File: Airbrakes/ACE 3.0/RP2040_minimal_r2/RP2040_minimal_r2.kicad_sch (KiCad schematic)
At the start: 45 parts, among them J1 USB_B_Micro, J2 Conn_01x02, J3 104031-0811, J4 Conn_02x18_Odd_Even, J5 104031-0811, U1 NCP1117-3.3_SOT223, U2 W25Q128JVS, U3 RP2040, U4 BMI088, U5 BMP581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

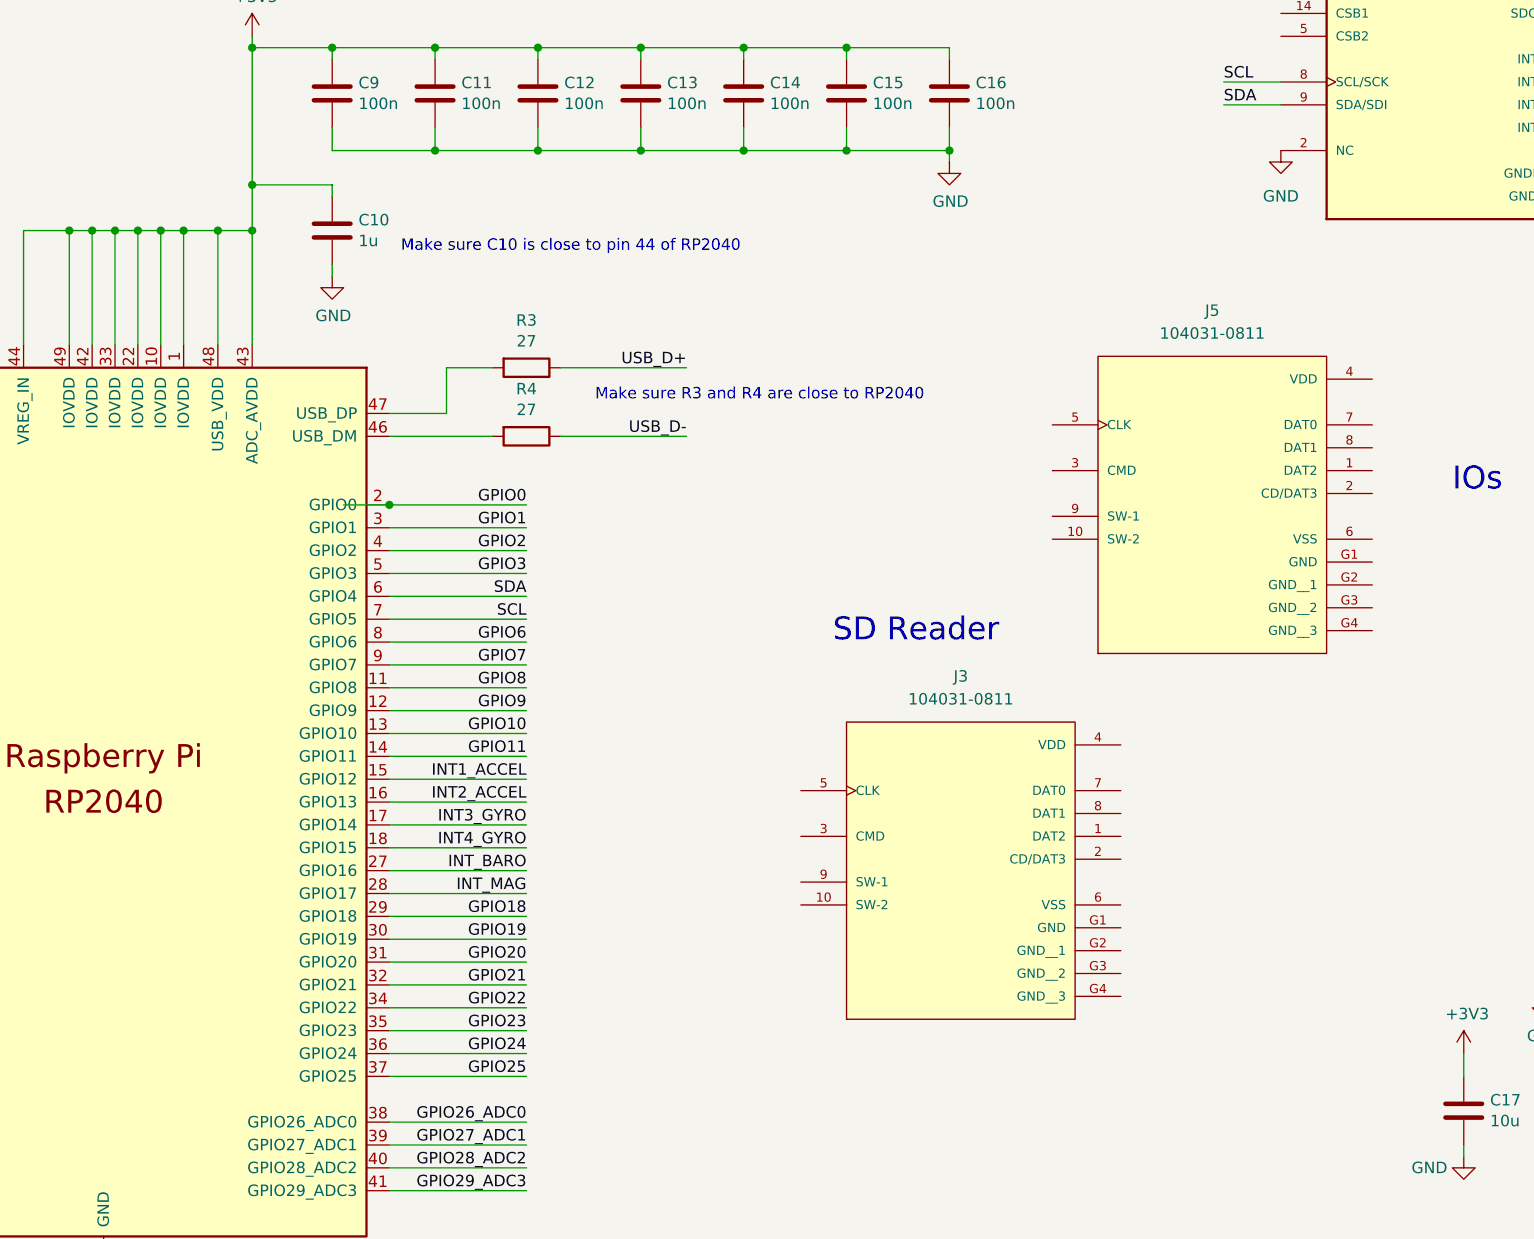
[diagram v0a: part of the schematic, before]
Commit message: sd card interfacing
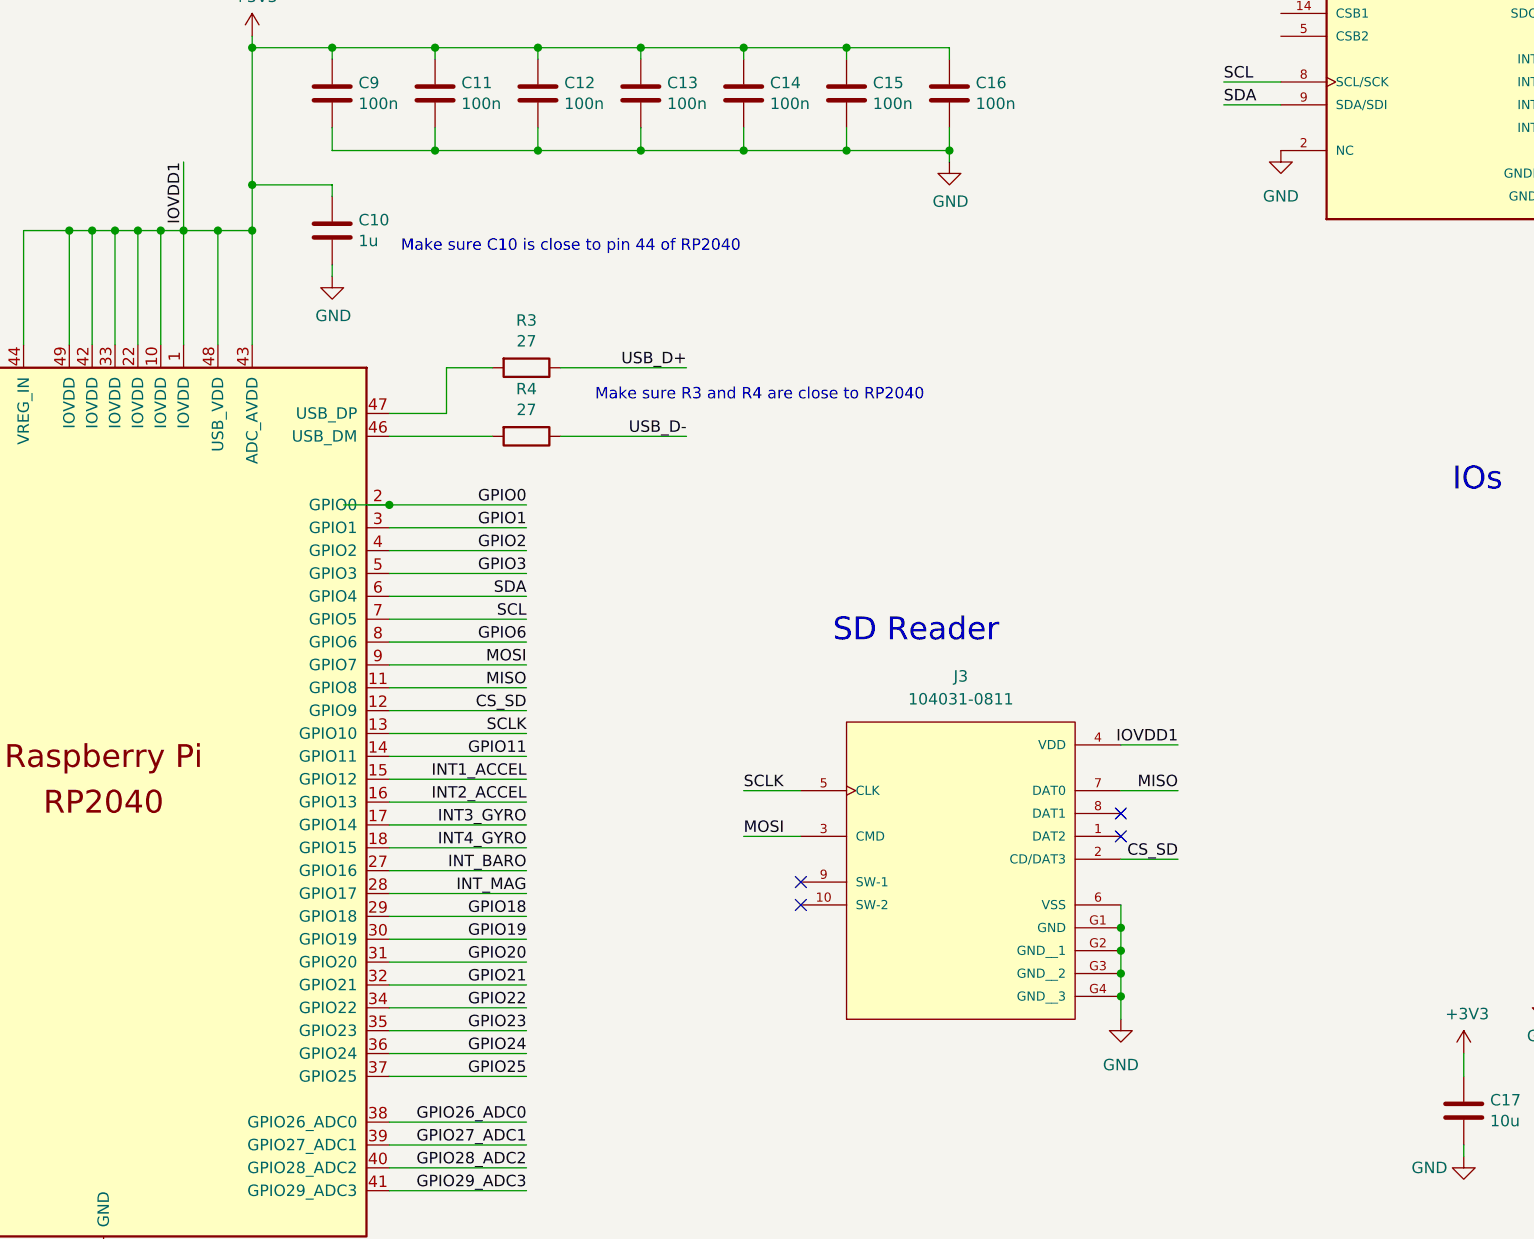
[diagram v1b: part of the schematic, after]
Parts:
- removed J5: 104031-0811, 1040310811-molex_usb:MOLEX_104031-0811, symbol 104031-0811:104031-0811
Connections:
- net GPIO10 is gone; now on net SCLK: U3.13 (GPIO10)
- net GPIO7 is gone; now on net MOSI: U3.9 (GPIO7)
- net GPIO8 is gone; now on net MISO: U3.11 (GPIO8)
- net GPIO9 is gone; now on net CS_SD: U3.12 (GPIO9)
- net +3V3: now also J3.4 (VDD)
- net GND: now also J3.6 (VSS), J3.G1 (GND), J3.G2 (GND__1), J3.G3 (GND__2), J3.G4 (GND__3)
- net CS_SD: now reaches J3.2 (CD/DAT3)
- net MOSI: now reaches J3.3 (CMD)
- net SCLK: now reaches J3.5 (CLK)
- net MISO: now reaches J3.7 (DAT0)
- no-connect marks 1 -> 5

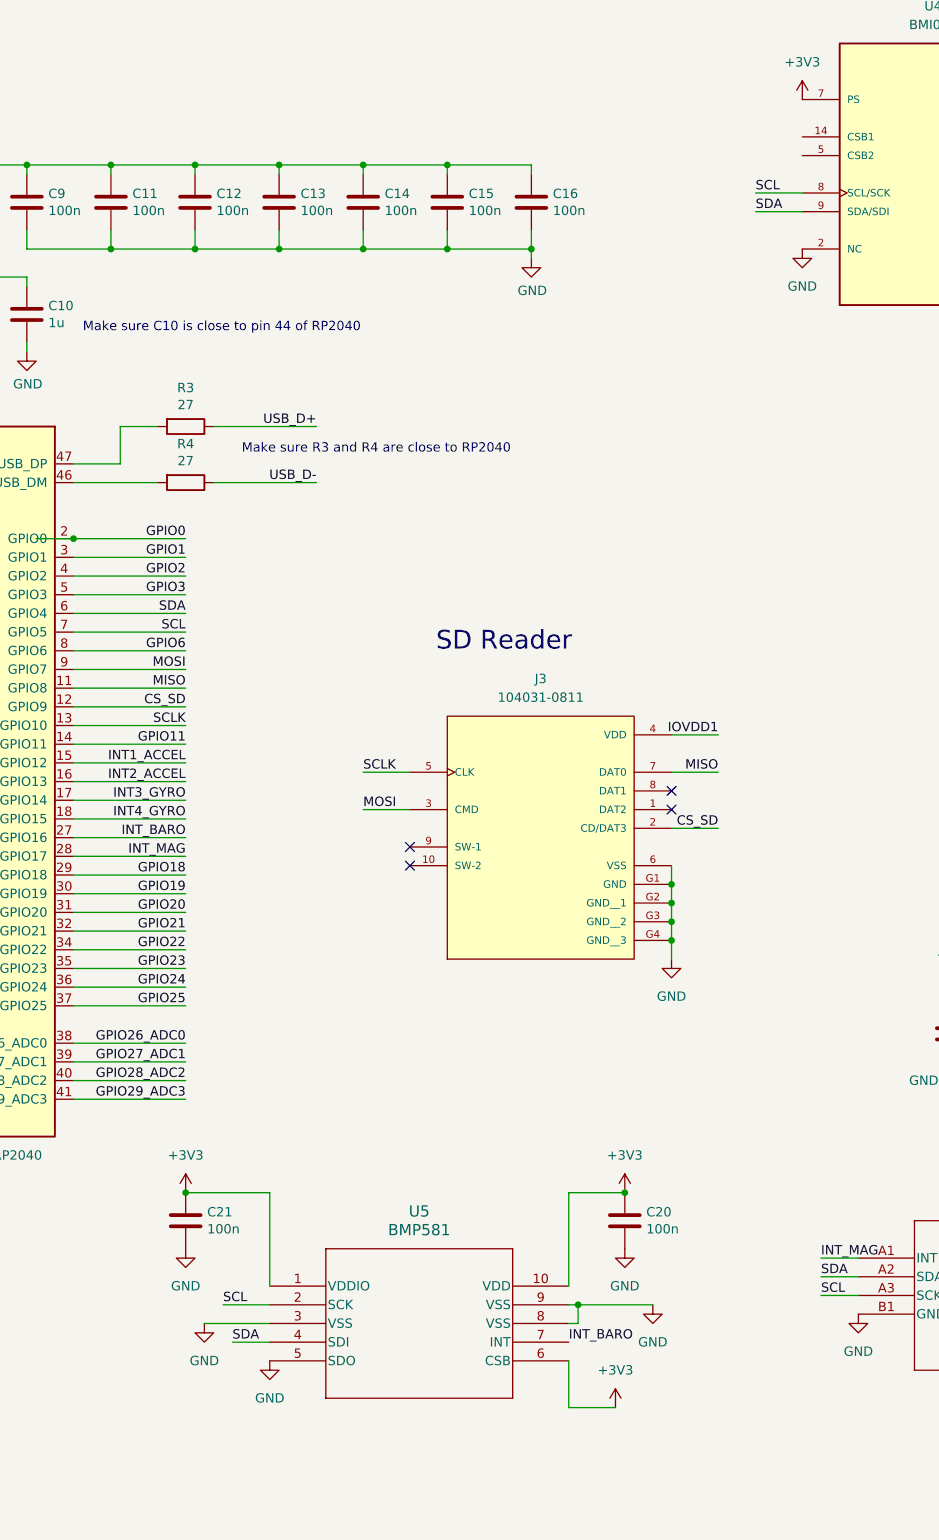
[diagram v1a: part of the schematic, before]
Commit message: changed cs_sd to pull-up and fixed csb
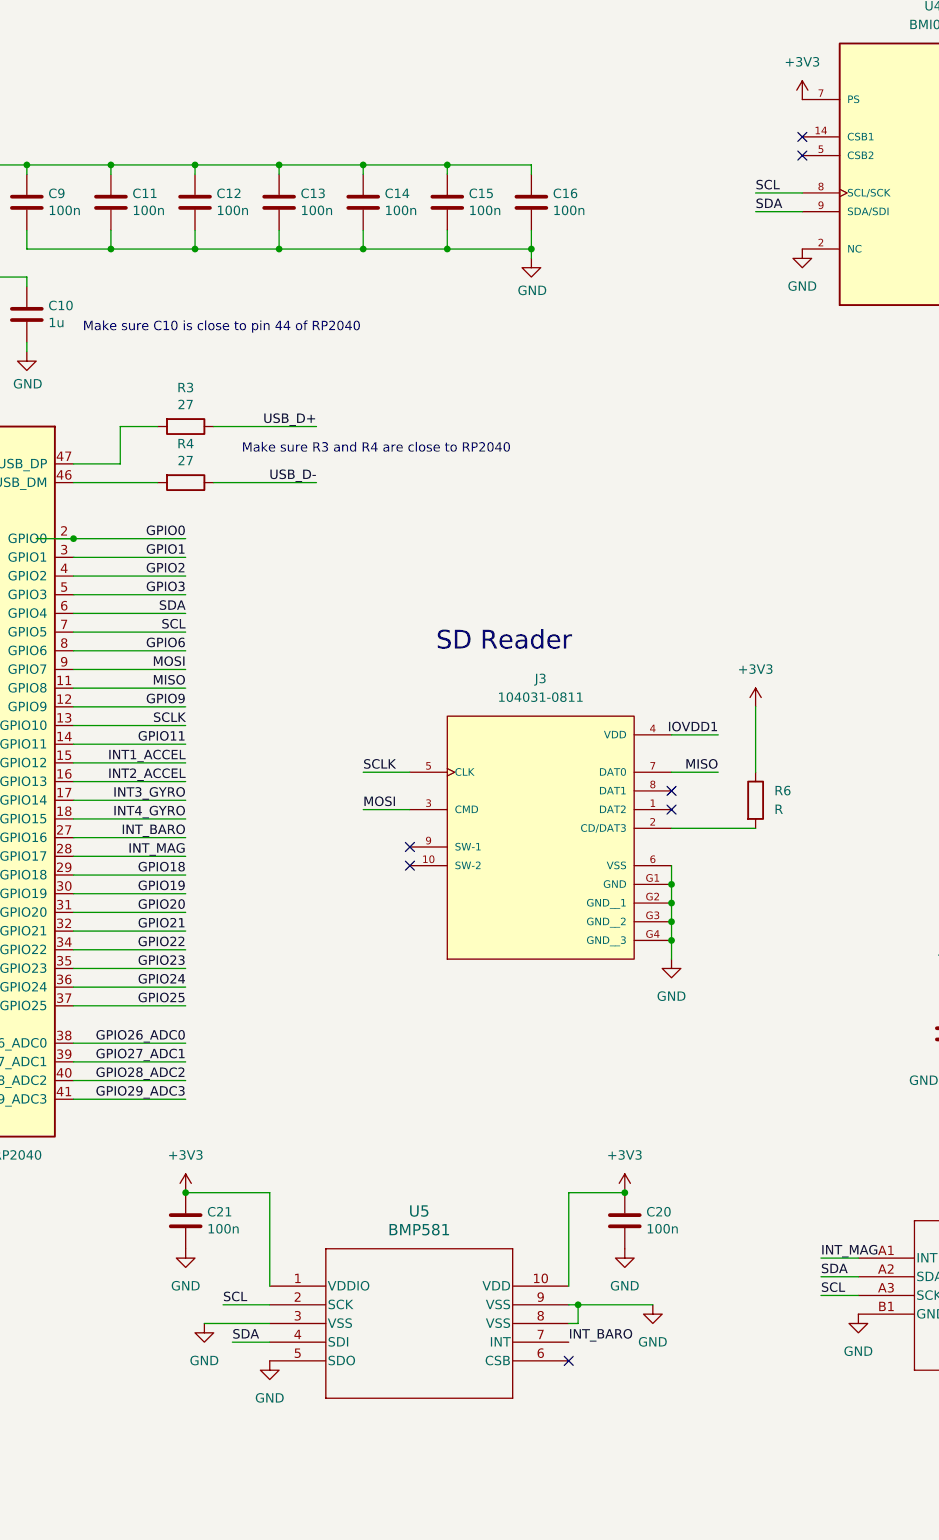
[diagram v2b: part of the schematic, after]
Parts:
- added R6: R, Resistor_SMD:R_0402_1005Metric, symbol Device:R
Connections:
- net +3V3: now also R6.1; no longer U5.6 (CSB)
- net CS_SD: no longer names the net of J3.2 (CD/DAT3)
- net CS_SD: now also R6.2; no longer U3.12 (GPIO9)
- new net GPIO9: U3.12 (GPIO9)
- no-connect marks 5 -> 8
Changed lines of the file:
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@@
 	)
 	(no_connect
+		(at 297.18 223.52)
+	)
+	(no_connect
 		(at 311.15 148.59)
 	)
@@
 	)
 	(no_connect
+		(at 328.93 57.15)
+	)
+	(no_connect
+		(at 328.93 59.69)
+	)
+	(no_connect
 		(at 311.15 146.05)
 	)
@@
 	(wire
 		(pts
-			(xy 297.18 223.52) (xy 297.18 229.87)
-		)
-		(stroke
-			(width 0)
-			(type default)
-		)
-	)
-	(wire
-		(pts
 			(xy 384.81 124.46) (xy 384.81 127)
 		)
@@
 	(wire
 		(pts
+			(xy 322.58 134.62) (xy 322.58 143.51)
+		)
+		(stroke
+			(width 0)
+			(type default)
+		)
+	)
+	(wire
+		(pts
 			(xy 297.18 215.9) (xy 298.45 215.9)
 		)
@@
 	(wire
 		(pts
-			(xy 297.18 229.87) (xy 303.53 229.87)
-		)
-		(stroke
-			(width 0)
-			(type default)
-		)
-	)
-	(wire
-		(pts
 			(xy 168.91 76.2) (xy 177.8 76.2)
 		)
@@
 	(wire
 		(pts
-			(xy 311.15 151.13) (xy 317.5 151.13)
+			(xy 311.15 151.13) (xy 322.58 151.13)
 		)
 		(stroke
@@
 		)
 	)
-	(label "CS_SD"
-		(at 317.5 151.13 180)
-		(fields_autoplaced yes)
-		(effects
-			(font
-				(size 1.27 1.27)
-			)
-			(justify right bottom)
-		)
-	)
 	(label "QSPI_SD2"
 		(at 152.4 121.92 0)
@@
 		)
 	)
-	(label "CS_SD"
+	(label "GPIO9"
 		(at 245.11 134.62 180)
 		(fields_autoplaced yes)
@@
 	)
 	(symbol
+		(lib_id "Device:R")
+		(at 322.58 147.32 0)
+		(unit 1)
+		(exclude_from_sim no)
+		(in_bom yes)
+		(on_board yes)
+		(dnp no)
+		(fields_autoplaced yes)
+		(property "Reference" "R6"
+			(at 325.12 146.0499 0)
+			(effects
+				(font
+					(size 1.27 1.27)
+				)
+				(justify left)
+			)
+		)
+		(property "Value" "R"
+			(at 325.12 148.5899 0)
+			(effects
+				(font
+					(size 1.27 1.27)
+				)
+				(justify left)
+			)
+		)
+		(property "Footprint" "Resistor_SMD:R_0402_1005Metric"
+			(at 320.802 147.32 90)
+			(effects
+				(font
+					(size 1.27 1.27)
+				)
+				(hide yes)
+			)
+		)
+		(property "Datasheet" "~"
+			(at 322.58 147.32 0)
+			(effects
+				(font
+					(size 1.27 1.27)
+				)
+				(hide yes)
+			)
+		)
+		(property "Description" "Resistor"
+			(at 322.58 147.32 0)
+			(effects
+				(font
+					(size 1.27 1.27)
+				)
+				(hide yes)
+			)
+		)
+		(pin "2"
+		)
+		(pin "1"
+		)
+		(instances
+			(project "RP2040_minimal_r2"
+				(path "/8c0b3d8b-46d3-4173-ab1e-a61765f77d61"
+					(reference "R6")
+					(unit 1)
+				)
+			)
+		)
+	)
+	(symbol
 		(lib_name "+3V3_6")
 		(lib_id "power:+3V3")
@@
 	)
 	(symbol
-		(lib_name "+3V3_5")
-		(lib_id "power:+3V3")
-		(at 303.53 229.87 0)
-		(unit 1)
-		(exclude_from_sim no)
-		(in_bom yes)
-		(on_board yes)
-		(dnp no)
-		(fields_autoplaced yes)
-		(property "Reference" "#PWR042"
-			(at 303.53 233.68 0)
-			(effects
-				(font
-					(size 1.27 1.27)
-				)
-				(hide yes)
-			)
-		)
-		(property "Value" "+3V3"
-			(at 303.53 224.79 0)
-			(effects
-				(font
-					(size 1.27 1.27)
-				)
-			)
-		)
-		(property "Footprint" ""
-			(at 303.53 229.87 0)
-			(effects
-				(font
-					(size 1.27 1.27)
-				)
-				(hide yes)
-			)
-		)
-		(property "Datasheet" ""
-			(at 303.53 229.87 0)
-			(effects
-				(font
-					(size 1.27 1.27)
-				)
-				(hide yes)
-			)
-		)
-		(property "Description" "Power symbol creates a global label with name \"+3V3\""
-			(at 303.53 229.87 0)
-			(effects
-				(font
-					(size 1.27 1.27)
-				)
-				(hide yes)
-			)
-		)
-		(pin "1"
-		)
-		(instances
-			(project "RP2040_minimal_r2"
-				(path "/8c0b3d8b-46d3-4173-ab1e-a61765f77d61"
-					(reference "#PWR042")
-					(unit 1)
-				)
-			)
-		)
-	)
-	(symbol
 		(lib_name "GND_9")
 		(lib_id "power:GND")
@@
 					(unit 1)
 				)
+			)
+		)
+	)
+	(symbol
+		(lib_name "+3V3_7")
+		(lib_id "power:+3V3")
+		(at 322.58 134.62 0)
+		(unit 1)
+		(exclude_from_sim no)
+		(in_bom yes)
+		(on_board yes)
+		(dnp no)
+		(fields_autoplaced yes)
+		(property "Reference" "#PWR020"
+			(at 322.58 138.43 0)
+			(effects
+				(font
+					(size 1.27 1.27)
+				)
+				(hide yes)
+			)
+		)
+		(property "Value" "+3V3"
+			(at 322.58 129.54 0)
+			(effects
+				(font
+					(size 1.27 1.27)
+				)
+			)
+		)
+		(property "Footprint" ""
+			(at 322.58 134.62 0)
+			(effects
+				(font
+					(size 1.27 1.27)
+				)
+				(hide yes)
+			)
+		)
+		(property "Datasheet" ""
+			(at 322.58 134.62 0)
+			(effects
+				(font
+					(size 1.27 1.27)
+				)
+				(hide yes)
+			)
+		)
+		(property "Description" "Power symbol creates a global label with name \"+3V3\""
+			(at 322.58 134.62 0)
+			(effects
+				(font
+					(size 1.27 1.27)
+				)
+				(hide yes)
+			)
+		)
+		(pin "1"
+		)
+		(instances
+			(project "RP2040_minimal_r2"
+				(path "/8c0b3d8b-46d3-4173-ab1e-a61765f77d61"
+					(reference "#PWR020")
+					(unit 1)
+				)

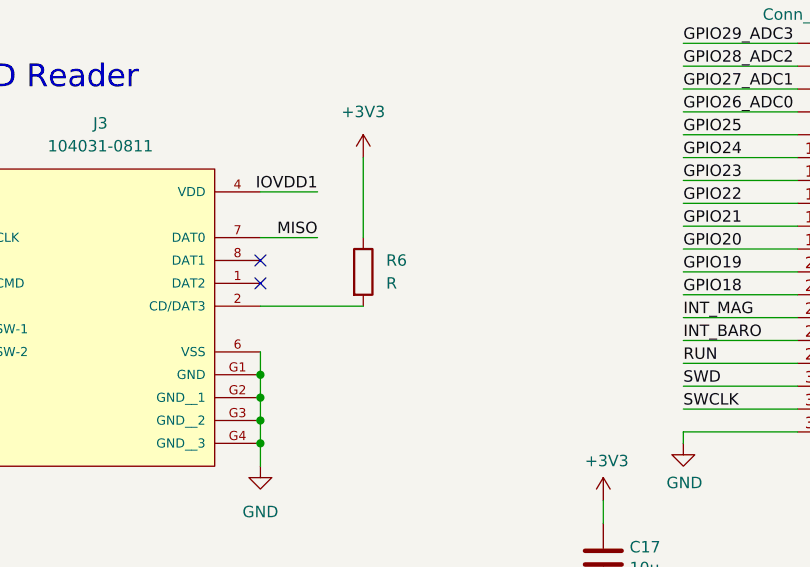
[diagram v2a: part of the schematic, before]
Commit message: Added resistor value for CS_SD pull up
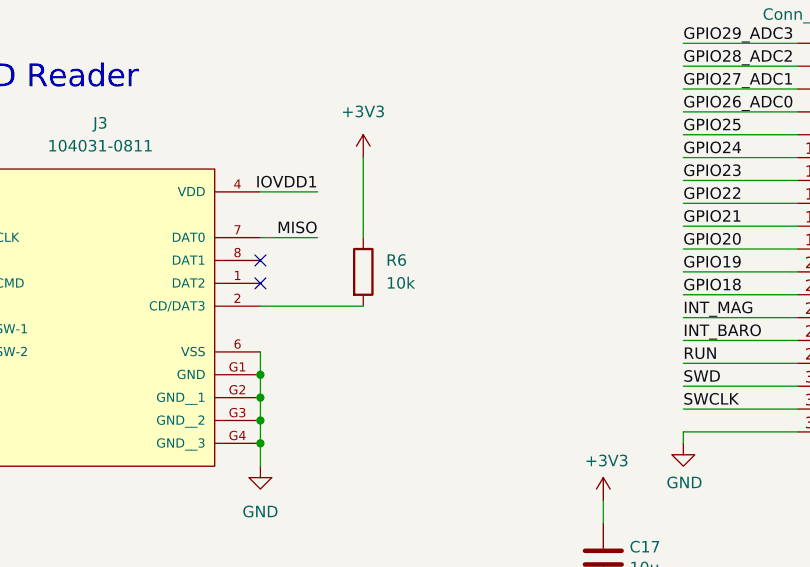
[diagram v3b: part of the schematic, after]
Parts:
- R6: value R -> 10k
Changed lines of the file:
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@@
 			)
 		)
-		(property "Value" "R"
+		(property "Value" "10k"
 			(at 325.12 148.5899 0)
 			(effects
